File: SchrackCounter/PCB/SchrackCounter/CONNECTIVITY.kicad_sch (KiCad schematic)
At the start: 6 parts

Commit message: Schematic update
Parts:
- gave numbers to parts that had none: 6
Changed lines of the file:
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@@
 		(on_board yes)
 		(dnp no)
-		(property "Reference" "R?"
+		(property "Reference" "R5"
 			(at 172.72 91.44 90)
 			(effects
@@
 			(project "SchrackCounter"
 				(path "/d96f2ffc-3f4c-4f71-b693-29f6b8c3245d/301b3ab9-8372-40d2-93c7-cd7607d23fc4"
-					(reference "R?")
+					(reference "R5")
 					(unit 1)
 				)
@@
 		(on_board yes)
 		(dnp no)
-		(property "Reference" "R?"
+		(property "Reference" "R4"
 			(at 172.72 66.04 90)
 			(effects
@@
 			(project "SchrackCounter"
 				(path "/d96f2ffc-3f4c-4f71-b693-29f6b8c3245d/301b3ab9-8372-40d2-93c7-cd7607d23fc4"
-					(reference "R?")
+					(reference "R4")
 					(unit 1)
 				)
@@
 		(dnp no)
 		(fields_autoplaced yes)
-		(property "Reference" "U?"
+		(property "Reference" "U8"
 			(at 200.66 62.23 0)
 			(effects
@@
 			(project "SchrackCounter"
 				(path "/d96f2ffc-3f4c-4f71-b693-29f6b8c3245d/301b3ab9-8372-40d2-93c7-cd7607d23fc4"
-					(reference "U?")
+					(reference "U8")
 					(unit 1)
 				)
@@
 		(on_board yes)
 		(dnp no)
-		(property "Reference" "D?"
+		(property "Reference" "D1"
 			(at 119.38 65.405 0)
 			(effects
@@
 			(project "SchrackCounter"
 				(path "/d96f2ffc-3f4c-4f71-b693-29f6b8c3245d/301b3ab9-8372-40d2-93c7-cd7607d23fc4"
-					(reference "D?")
+					(reference "D1")
 					(unit 1)
 				)
@@
 		(on_board yes)
 		(dnp no)
-		(property "Reference" "C?"
+		(property "Reference" "C13"
 			(at 226.06 86.36 0)
 			(effects
@@
 			(project "SchrackCounter"
 				(path "/d96f2ffc-3f4c-4f71-b693-29f6b8c3245d/301b3ab9-8372-40d2-93c7-cd7607d23fc4"
-					(reference "C?")
+					(reference "C13")
 					(unit 1)
 				)
@@
 		(on_board yes)
 		(dnp no)
-		(property "Reference" "J?"
+		(property "Reference" "J1"
 			(at 144.78 64.77 0)
 			(effects
@@
 			(project "SchrackCounter"
 				(path "/d96f2ffc-3f4c-4f71-b693-29f6b8c3245d/301b3ab9-8372-40d2-93c7-cd7607d23fc4"
-					(reference "J?")
+					(reference "J1")
 					(unit 1)
 				)

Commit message: Schematic update
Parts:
- added BZ?: Buzzer, symbol Device:Buzzer
- added D? (x8): LED, symbol Device:LED
- added R? (x8): 220R, symbol Device:R
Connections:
- new net: D?.2 (A), R?.2 (x8)
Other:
- note added: "current in parallel Max GPIO current 40mA, recommended 20mA"
- moved on the sheet: C13, D1, J1, R4, R5, U8

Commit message: sleep, overated imo
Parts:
- removed D? (x4): LED, symbol Device:LED
- removed R? (x8): 220R, symbol Device:R
- added D6, D7, D8, D9: LED, LED_SMD:LED_0805_2012Metric_Pad1.15x1.40mm_HandSolder, symbol Device:LED
- added R4, R5, R8, R9: 220R, Resistor_SMD:R_0805_2012Metric_Pad1.20x1.40mm_HandSolder, symbol Device:R
- BZ1: renamed from BZ?; footprint (none) -> Schrack_brd:CUI_CPT-1625-80
- D2, D3, D4, D5: renamed from D?; footprint (none) -> LED_SMD:LED_0805_2012Metric_Pad1.15x1.40mm_HandSolder
- renumbered R4 to R6, R5 to R7
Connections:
- net GND: now also BZ1.2 (-), D2.1 (K), D3.1 (K), D4.1 (K), D5.1 (K), D6.1 (K), D7.1 (K), D8.1 (K), D9.1 (K)
- net at D4.2 (A): now also D5.2 (A), R5.2
- net BZ1_PWM: now reaches BZ1.1 (+)
- net at D2.2 (A): now also D3.2 (A), R4.2
- new net: D6.2 (A), D7.2 (A), R8.2
- new net: D8.2 (A), D9.2 (A), R9.2
- new net GREEN_FLASH: R4.1, R5.1
- new net RED_FLASH: R8.1, R9.1
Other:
- note added: "Funny bug, show to nat >:3"
- note added: "SIGNALING"
- moved on the sheet: BZ1, C13, D1, D2, D3, D4, D5, J1, R6, R7, U8

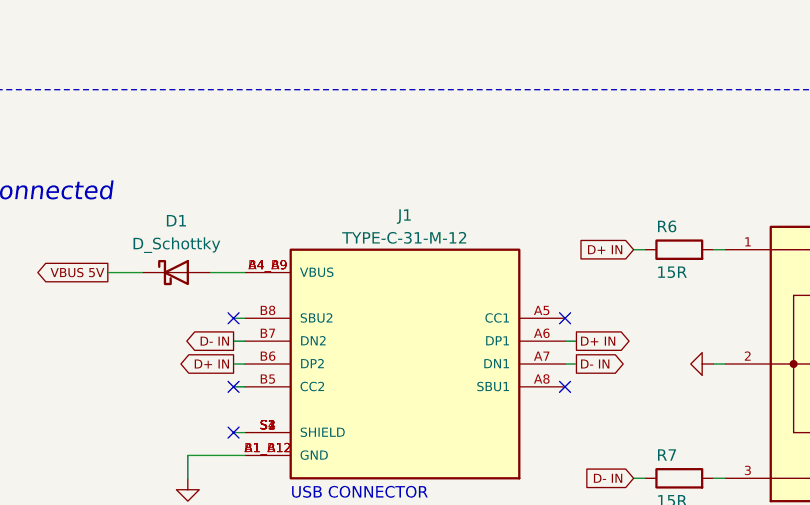
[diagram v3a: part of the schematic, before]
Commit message: Footprint reorder, schematic and pcb update
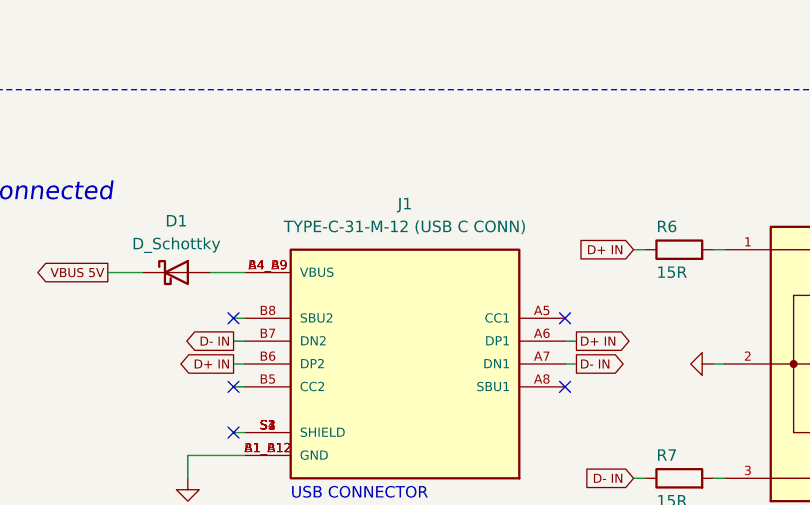
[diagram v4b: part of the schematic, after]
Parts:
- removed J1: TYPE-C-31-M-12, sumec-smdV2_library:USB_Type_C, symbol sumec_library:TYPE-C-31-M-12
- added J1: TYPE-C-31-M-12 (USB C CONN), sumec_brd:USB_Type_C, symbol SchrackThingy_library:TYPE-C-31-M-12 (USB C CONN)
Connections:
- net D+ IN: now also J1.A6 (DP1), J1.B6 (DP2)
- net D- IN: now also J1.A7 (DN1), J1.B7 (DN2)
- net GND: now also J1.A1_B12 (GND), J1.B1_A12 (GND)
- net at D1.2 (A): now also J1.A4_B9 (VBUS), J1.B4_A9 (VBUS)
- new net: J1.S1 (SHIELD), J1.S2 (SHIELD), J1.S3 (SHIELD), J1.S4 (SHIELD)
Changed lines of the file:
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@@
+	)
+	(symbol
+		(lib_id "SchrackThingy_library:TYPE-C-31-M-12 (USB C CONN)")
+		(at 146.05 62.23 0)
+		(mirror y)
+		(unit 1)
+		(exclude_from_sim no)
+		(in_bom yes)
+		(on_board yes)
+		(dnp no)
+		(property "Reference" "J1"
+			(at 146.05 44.45 0)
+			(effects
+				(font
+					(size 1.27 1.27)
+				)
+			)
+		)
+		(property "Value" "TYPE-C-31-M-12 (USB C CONN)"
+			(at 146.05 46.99 0)
+			(effects
+				(font
+					(size 1.27 1.27)
+				)
+			)
+		)
+		(property "Footprint" "sumec_brd:USB_Type_C"
+			(at 146.05 62.23 0)
+			(effects
+				(font
+					(size 1.27 1.27)
+				)
+				(justify bottom)
+				(hide yes)
+			)
+		)
+		(property "Datasheet" ""
+			(at 146.05 62.23 0)
+			(effects
+				(font
+					(size 1.27 1.27)
+				)
+				(hide yes)
+			)
+		)
+		(property "Description" "USB Connectors 24 Receptacle 1 8.94*7.3mm RoHS"
+			(at 146.05 62.23 0)
+			(effects
+				(font
+					(size 1.27 1.27)
+				)
+				(justify bottom)
+				(hide yes)
+			)
+		)
+		(property "MF" "HRO Electronics Co., Ltd."
+			(at 146.05 62.23 0)
+			(effects
+				(font
+					(size 1.27 1.27)
+				)
+				(justify bottom)
+				(hide yes)
+			)
+		)
+		(property "MAXIMUM_PACKAGE_HEIGHT" "3.26 mm"
+			(at 146.05 62.23 0)
+			(effects
+				(font
+					(size 1.27 1.27)
+				)
+				(justify bottom)
+				(hide yes)
+			)
+		)
+		(property "Package" "Package"
+			(at 146.05 62.23 0)
+			(effects
+				(font
+					(size 1.27 1.27)
+				)
+				(justify bottom)
+				(hide yes)
+			)
+		)
+		(property "Price" "None"
+			(at 146.05 62.23 0)
+			(effects
+				(font
+					(size 1.27 1.27)
+				)
+				(justify bottom)
+				(hide yes)
+			)
+		)
+		(property "Check_prices" "https://www.snapeda.com/parts/TYPE-C-31-M-12/HRO+Electronics+Co.%252C+Ltd./view-part/?ref=eda"
+			(at 143.51 62.23 0)
+			(effects
+				(font
+					(size 1.27 1.27)
+				)
+				(justify bottom)
+				(hide yes)
+			)
+		)
+		(property "STANDARD" "Manufacturer Recommendations"
+			(at 146.05 62.23 0)
+			(effects
+				(font
+					(size 1.27 1.27)
+				)
+				(justify bottom)
+				(hide yes)
+			)
+		)
+		(property "PARTREV" "2020.12.08"
+			(at 146.05 62.23 0)
+			(effects
+				(font
+					(size 1.27 1.27)
+				)
+				(justify bottom)
+				(hide yes)
+			)
+		)
+		(property "SnapEDA_Link" "https://www.snapeda.com/parts/TYPE-C-31-M-12/HRO+Electronics+Co.%252C+Ltd./view-part/?ref=snap"
+			(at 146.05 62.23 0)
+			(effects
+				(font
+					(size 1.27 1.27)
+				)
+				(justify bottom)
+				(hide yes)
+			)
+		)
+		(property "MP" "TYPE-C-31-M-12"
+			(at 146.05 62.23 0)
+			(effects
+				(font
+					(size 1.27 1.27)
+				)
+				(justify bottom)
+				(hide yes)
+			)
+		)
+		(property "SNAPEDA_PN" "TYPE-C-31-M-12"
+			(at 146.05 62.23 0)
+			(effects
+				(font
+					(size 1.27 1.27)
+				)
+				(justify bottom)
+				(hide yes)
+			)
+		)
+		(property "Availability" "Not in stock"
+			(at 146.05 62.23 0)
+			(effects
+				(font
+					(size 1.27 1.27)
+				)
+				(justify bottom)
+				(hide yes)
+			)
+		)
+		(property "MANUFACTURER" "HRO Electronics Co., Ltd."
+			(at 146.05 62.23 0)
+			(effects
+				(font
+					(size 1.27 1.27)
+				)
+				(justify bottom)
+				(hide yes)
+			)
+		)
+		(pin "A5"
+		)
+		(pin "A6"
+		)
+		(pin "B5"
+		)
+		(pin "S1"
+		)
+		(pin "S2"
+		)
+		(pin "A7"
+		)
+		(pin "B7"
+		)
+		(pin "A8"
+		)
+		(pin "B4_A9"
+		)
+		(pin "A4_B9"
+		)
+		(pin "B6"
+		)
+		(pin "S3"
+		)
+		(pin "S4"
+		)
+		(pin "A1_B12"
+		)
+		(pin "B8"
+		)
+		(pin "B1_A12"
+		)
+		(instances
+			(project "SchrackCounter"
+				(path "/d96f2ffc-3f4c-4f71-b693-29f6b8c3245d/301b3ab9-8372-40d2-93c7-cd7607d23fc4"
+					(reference "J1")
+					(unit 1)
+				)
+			)
+		)
 	)
 	(symbol
@@
 					(unit 1)
 				)
-			)
-		)
-	)
-	(symbol
-		(lib_id "sumec_library:TYPE-C-31-M-12")
-		(at 146.05 62.23 0)
-		(mirror y)
-		(unit 1)
-		(exclude_from_sim no)
-		(in_bom yes)
-		(on_board yes)
-		(dnp no)
-		(property "Reference" "J1"
-			(at 146.05 45.72 0)
-			(effects
-				(font
-					(face "Bahnschrift")
-					(size 1.27 1.27)
-				)
-			)
-		)
-		(property "Value" "TYPE-C-31-M-12"
-			(at 146.05 48.26 0)
-			(effects
-				(font
-					(face "Bahnschrift")
-					(size 1.27 1.27)
-				)
-			)
-		)
-		(property "Footprint" "sumec-smdV2_library:USB_Type_C"
-			(at 146.05 62.23 0)
-			(effects
-				(font
-					(face "Bahnschrift")
-					(size 1.27 1.27)
-				)
-				(justify bottom)
-				(hide yes)
-			)
-		)
-		(property "Datasheet" ""
-			(at 146.05 62.23 0)
-			(effects
-				(font
-					(face "Bahnschrift")
-					(size 1.27 1.27)
-				)
-				(hide yes)
-			)
-		)
-		(property "Description" "\nUSB Connectors 24 Receptacle 1 8.94*7.3mm RoHS\n"
-			(at 146.05 62.23 0)
-			(effects
-				(font
-					(face "Bahnschrift")
-					(size 1.27 1.27)
-				)
-				(justify bottom)
-				(hide yes)
-			)
-		)
-		(property "MF" "HRO Electronics Co., Ltd."
-			(at 146.05 62.23 0)
-			(effects
-				(font
-					(face "Bahnschrift")
-					(size 1.27 1.27)
-				)
-				(justify bottom)
-				(hide yes)
-			)
-		)
-		(property "MAXIMUM_PACKAGE_HEIGHT" "3.26 mm"
-			(at 146.05 62.23 0)
-			(effects
-				(font
-					(face "Bahnschrift")
-					(size 1.27 1.27)
-				)
-				(justify bottom)
-				(hide yes)
-			)
-		)
-		(property "Package" "Package"
-			(at 146.05 62.23 0)
-			(effects
-				(font
-					(face "Bahnschrift")
-					(size 1.27 1.27)
-				)
-				(justify bottom)
-				(hide yes)
-			)
-		)
-		(property "Price" "None"
-			(at 146.05 62.23 0)
-			(effects
-				(font
-					(face "Bahnschrift")
-					(size 1.27 1.27)
-				)
-				(justify bottom)
-				(hide yes)
-			)
-		)
-		(property "Check_prices" "https://www.snapeda.com/parts/TYPE-C-31-M-12/HRO+Electronics+Co.%252C+Ltd./view-part/?ref=eda"
-			(at 146.05 62.23 0)
-			(effects
-				(font
-					(face "Bahnschrift")
-					(size 1.27 1.27)
-				)
-				(justify bottom)
-				(hide yes)
-			)
-		)
-		(property "STANDARD" "Manufacturer Recommendations"
-			(at 146.05 62.23 0)
-			(effects
-				(font
-					(face "Bahnschrift")
-					(size 1.27 1.27)
-				)
-				(justify bottom)
-				(hide yes)
-			)
-		)
-		(property "PARTREV" "2020.12.08"
-			(at 146.05 62.23 0)
-			(effects
-				(font
-					(face "Bahnschrift")
-					(size 1.27 1.27)
-				)
-				(justify bottom)
-				(hide yes)
-			)
-		)
-		(property "SnapEDA_Link" "https://www.snapeda.com/parts/TYPE-C-31-M-12/HRO+Electronics+Co.%252C+Ltd./view-part/?ref=snap"
-			(at 146.05 62.23 0)
-			(effects
-				(font
-					(face "Bahnschrift")
-					(size 1.27 1.27)
-				)
-				(justify bottom)
-				(hide yes)
-			)
-		)
-		(property "MP" "TYPE-C-31-M-12"
-			(at 146.05 62.23 0)
-			(effects
-				(font
-					(face "Bahnschrift")
-					(size 1.27 1.27)
-				)
-				(justify bottom)
-				(hide yes)
-			)
-		)
-		(property "SNAPEDA_PN" "TYPE-C-31-M-12"
-			(at 146.05 62.23 0)
-			(effects
-				(font
-					(face "Bahnschrift")
-					(size 1.27 1.27)
-				)
-				(justify bottom)
-				(hide yes)
-			)
-		)
-		(property "Availability" "Not in stock"
-			(at 146.05 62.23 0)
-			(effects
-				(font
-					(face "Bahnschrift")
-					(size 1.27 1.27)
-				)
-				(justify bottom)
-				(hide yes)
-			)
-		)
-		(property "MANUFACTURER" "HRO Electronics Co., Ltd."
-			(at 146.05 62.23 0)
-			(effects
-				(font
-					(face "Bahnschrift")
-					(size 1.27 1.27)
-				)
-				(justify bottom)
-				(hide yes)
-			)
-		)
-		(pin "A1_B12"
-		)
-		(pin "A4_B9"
-		)
-		(pin "A5"
-		)
-		(pin "A6"
-		)
-		(pin "A7"
-		)
-		(pin "A8"
-		)
-		(pin "B1_A12"
-		)
-		(pin "B4_A9"
-		)
-		(pin "B5"
-		)
-		(pin "B6"
-		)
-		(pin "B7"
-		)
-		(pin "B8"
-		)
-		(pin "S1"
-		)
-		(pin "S2"
-		)
-		(pin "S3"
-		)
-		(pin "S4"
-		)
-		(instances
-			(project "SchrackCounter"
-				(path "/d96f2ffc-3f4c-4f71-b693-29f6b8c3245d/301b3ab9-8372-40d2-93c7-cd7607d23fc4"
-					(reference "J1")
-					(unit 1)
-				)

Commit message: PCB update
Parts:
- BZ1: footprint Schrack_brd:CUI_CPT-1625-80 -> Schrack_brd:BUZZER_CUI_CPT
- renumbered J1 to J2, U8 to U6
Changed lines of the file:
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@@
 			)
 		)
-		(property "Footprint" "Schrack_brd:CUI_CPT-1625-80"
+		(property "Footprint" "Schrack_brd:BUZZER_CUI_CPT"
 			(at 127 130.175 90)
 			(effects
@@
 		(dnp no)
 		(fields_autoplaced yes)
-		(property "Reference" "#PWR028"
+		(property "Reference" "#PWR026"
 			(at 173.99 62.23 0)
 			(effects
@@
 			(project "SchrackCounter"
 				(path "/d96f2ffc-3f4c-4f71-b693-29f6b8c3245d/301b3ab9-8372-40d2-93c7-cd7607d23fc4"
-					(reference "#PWR028")
+					(reference "#PWR026")
 					(unit 1)
 				)
@@
 		(dnp no)
 		(fields_autoplaced yes)
-		(property "Reference" "#PWR029"
+		(property "Reference" "#PWR027"
 			(at 181.61 154.94 0)
 			(effects
@@
 			(project "SchrackCounter"
 				(path "/d96f2ffc-3f4c-4f71-b693-29f6b8c3245d/301b3ab9-8372-40d2-93c7-cd7607d23fc4"
-					(reference "#PWR029")
+					(reference "#PWR027")
 					(unit 1)
 				)
@@
 		(dnp no)
 		(fields_autoplaced yes)
-		(property "Reference" "#PWR026"
+		(property "Reference" "#PWR024"
 			(at 121.92 81.28 0)
 			(effects
@@
 			(project "SchrackCounter"
 				(path "/d96f2ffc-3f4c-4f71-b693-29f6b8c3245d/301b3ab9-8372-40d2-93c7-cd7607d23fc4"
-					(reference "#PWR026")
+					(reference "#PWR024")
 					(unit 1)
 				)
@@
 		(on_board yes)
 		(dnp no)
-		(property "Reference" "J1"
+		(property "Reference" "J2"
 			(at 146.05 44.45 0)
 			(effects
@@
 			(project "SchrackCounter"
 				(path "/d96f2ffc-3f4c-4f71-b693-29f6b8c3245d/301b3ab9-8372-40d2-93c7-cd7607d23fc4"
-					(reference "J1")
+					(reference "J2")
 					(unit 1)
 				)
@@
 		(dnp no)
 		(fields_autoplaced yes)
-		(property "Reference" "#PWR027"
+		(property "Reference" "#PWR025"
 			(at 138.43 138.43 0)
 			(effects
@@
 			(project "SchrackCounter"
 				(path "/d96f2ffc-3f4c-4f71-b693-29f6b8c3245d/301b3ab9-8372-40d2-93c7-cd7607d23fc4"
-					(reference "#PWR027")
+					(reference "#PWR025")
 					(unit 1)
 				)
@@
 		(dnp no)
 		(fields_autoplaced yes)
-		(property "Reference" "U8"
+		(property "Reference" "U6"
 			(at 201.93 43.18 0)
 			(effects
@@
 			(project "SchrackCounter"
 				(path "/d96f2ffc-3f4c-4f71-b693-29f6b8c3245d/301b3ab9-8372-40d2-93c7-cd7607d23fc4"
-					(reference "U8")
+					(reference "U6")
 					(unit 1)
 				)
@@
 		(dnp no)
 		(fields_autoplaced yes)
-		(property "Reference" "#PWR031"
+		(property "Reference" "#PWR029"
 			(at 223.52 154.94 0)
 			(effects
@@
 			(project "SchrackCounter"
 				(path "/d96f2ffc-3f4c-4f71-b693-29f6b8c3245d/301b3ab9-8372-40d2-93c7-cd7607d23fc4"
-					(reference "#PWR031")
+					(reference "#PWR029")
 					(unit 1)
 				)
@@
 		(dnp no)
 		(fields_autoplaced yes)
-		(property "Reference" "#PWR030"
+		(property "Reference" "#PWR028"
 			(at 223.52 77.47 0)
 			(effects
@@
 			(project "SchrackCounter"
 				(path "/d96f2ffc-3f4c-4f71-b693-29f6b8c3245d/301b3ab9-8372-40d2-93c7-cd7607d23fc4"
-					(reference "#PWR030")
-					(unit 1)
-				)
+					(reference "#PWR028")
+					(unit 1)
+				)

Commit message: schematic and board update
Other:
- note removed: "Funny bug, show to nat >:3"
- moved on the sheet: BZ1
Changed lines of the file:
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@@
 	(wire
 		(pts
-			(xy 132.08 138.43) (xy 132.08 132.08)
+			(xy 134.62 137.16) (xy 134.62 132.08)
 		)
 		(stroke
@@
 	(wire
 		(pts
-			(xy 127 137.16) (xy 127 132.08)
+			(xy 129.54 137.16) (xy 129.54 132.08)
 		)
 		(stroke
@@
 			)
 			(justify left)
-		)
-	)
-	(text "Funny bug, show to nat >:3"
-		(exclude_from_sim no)
-		(at 128.905 142.875 0)
-		(effects
-			(font
-				(size 1.27 1.27)
-				(color 194 0 194 1)
-			)
 		)
 	)
@@
 	(global_label "BZ1_PWM"
 		(shape input)
-		(at 127 137.16 180)
+		(at 129.54 137.16 180)
 		(fields_autoplaced yes)
 		(effects
@@
 		)
 		(property "Intersheetrefs" "${INTERSHEET_REFS}"
-			(at 118.9317 137.16 0)
+			(at 121.4717 137.16 0)
 			(effects
 				(font
@@
 	(symbol
 		(lib_id "Device:Buzzer")
-		(at 129.54 129.54 90)
+		(at 132.08 129.54 90)
 		(unit 1)
 		(exclude_from_sim no)
@@
 		(dnp no)
 		(property "Reference" "BZ1"
-			(at 128.2699 125.73 0)
+			(at 132.08 122.555 90)
 			(effects
 				(font
@@
 		)
 		(property "Value" "Buzzer"
-			(at 130.8099 125.73 0)
+			(at 134.9375 124.7776 90)
 			(effects
 				(font
@@
 		)
 		(property "Footprint" "Schrack_brd:BUZZER_CUI_CPT"
-			(at 127 130.175 90)
+			(at 129.54 130.175 90)
 			(effects
 				(font
@@
 		)
 		(property "Datasheet" "https://cz.mouser.com/ProductDetail/CUI-Devices/CPT-1625-80-SMT-TR?qs=P1JMDcb91o43eCFIymFs3Q%3D%3D"
-			(at 127 130.175 90)
+			(at 129.54 130.175 90)
 			(effects
 				(font
@@
 		)
 		(property "Description" "Buzzer, polarized"
-			(at 129.54 129.54 0)
+			(at 132.08 129.54 0)
 			(effects
 				(font
@@
 	(symbol
 		(lib_id "power:GND")
-		(at 132.08 138.43 90)
+		(at 134.62 137.16 0)
 		(unit 1)
 		(exclude_from_sim no)
@@
 		(fields_autoplaced yes)
 		(property "Reference" "#PWR025"
-			(at 138.43 138.43 0)
+			(at 134.62 143.51 0)
 			(effects
 				(font
@@
 		)
 		(property "Value" "GND"
-			(at 135.89 139.065 90)
+			(at 133.985 140.97 90)
 			(effects
 				(font
@@
 		)
 		(property "Footprint" ""
-			(at 132.08 138.43 0)
+			(at 134.62 137.16 0)
 			(effects
 				(font
@@
 		)
 		(property "Datasheet" ""
-			(at 132.08 138.43 0)
+			(at 134.62 137.16 0)
 			(effects
 				(font
@@
 		)
 		(property "Description" ""
-			(at 132.08 138.43 0)
-			(effects
-				(font
+			(at 134.62 137.16 0)
+			(effects
+				(font
